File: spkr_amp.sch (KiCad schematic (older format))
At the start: 3 parts

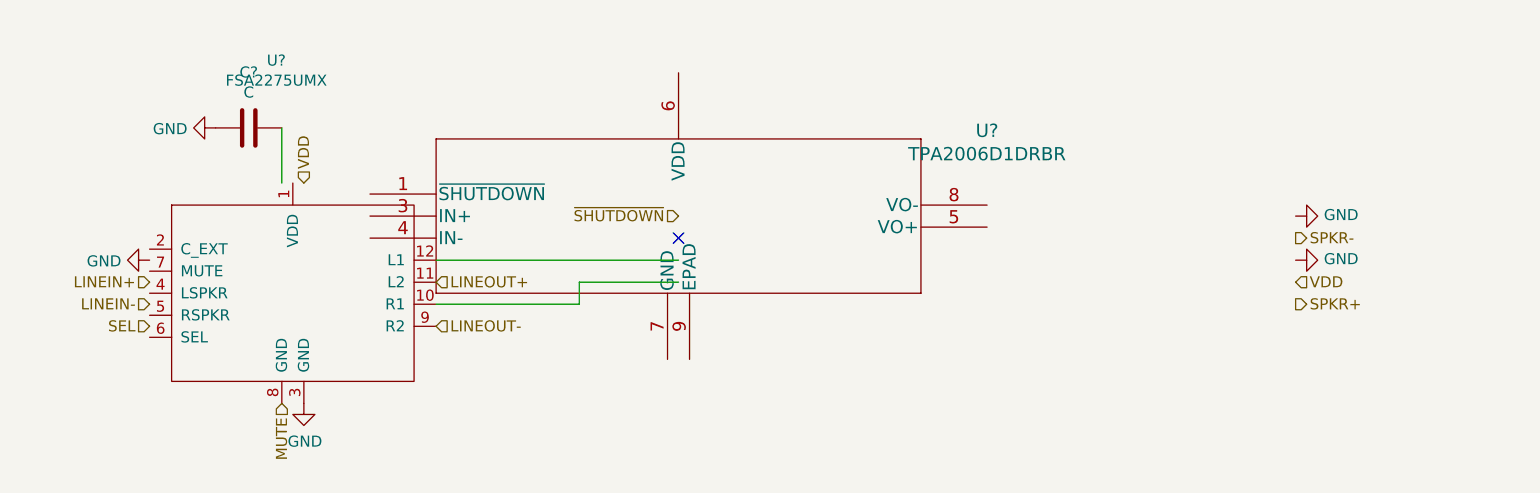
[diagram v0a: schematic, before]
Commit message: Import FSA2275 footprint from SnapEDA; annotate symbols.
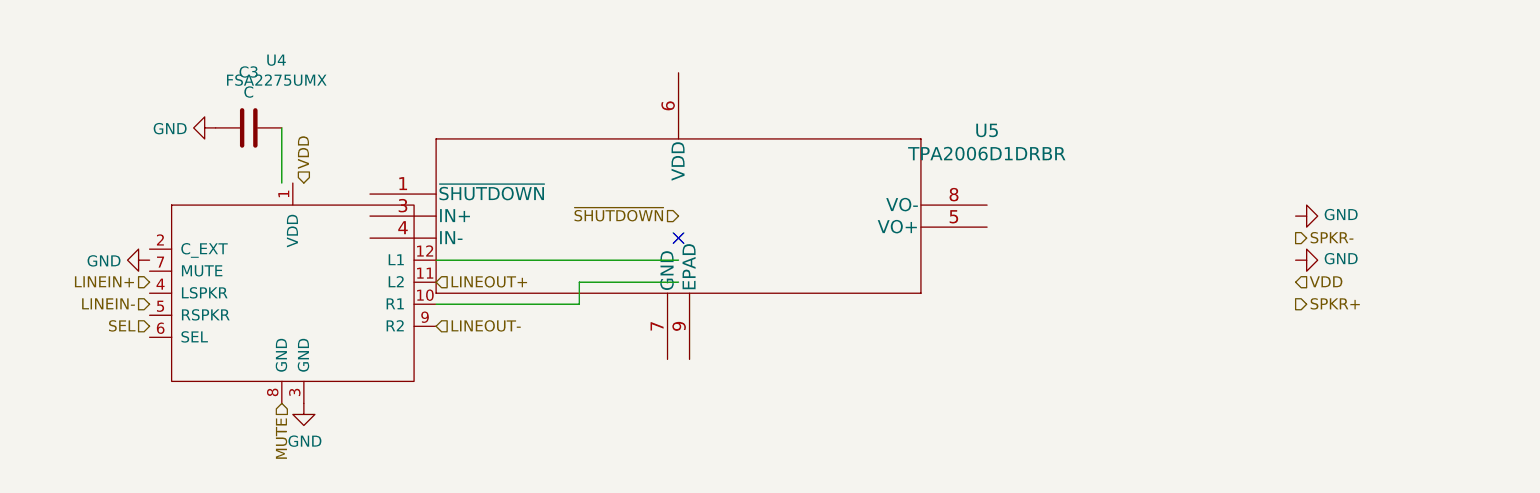
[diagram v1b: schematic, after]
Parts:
- C2: renamed from C?; footprint (none) -> Capacitor_SMD:C_0402_1005Metric
- U2: renamed from U?; footprint (none) -> footprints:FSA2275
- U3: renamed from U?; footprint DRB8_1P75X1P5 -> footprints:TPA2006D1DRBR
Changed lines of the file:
@@
 $Descr A4 11693 8268
 encoding utf-8
-Sheet 2 3
+Sheet 3 3
 Title ""
 Date ""
@@
 P 5500 3300
 AR Path="/6026AF34" Ref="U?"  Part="1"
-AR Path="/6026A3BE/6026AF34" Ref="U?"  Part="1"
-AR Path="/60276BEA/6026AF34" Ref="U?"  Part="1"
-F 0 "U?" H 6900 3687 60  0000 C CNN
+AR Path="/6026A3BE/6026AF34" Ref="U3"  Part="1"
+AR Path="/60276BEA/6026AF34" Ref="U5"  Part="1"
+F 0 "U5" H 6900 3687 60  0000 C CNN
 F 1 "TPA2006D1DRBR" H 6900 3581 60  0000 C CNN
-F 2 "DRB8_1P75X1P5" H 6900 3540 60  0001 C CNN
+F 2 "footprints:TPA2006D1DRBR" H 6900 3540 60  0001 C CNN
 F 3 "" H 5500 3300 60  0000 C CNN
 	1    5500 3300
@@
 P 3750 3650
 AR Path="/6026AF3A" Ref="U?"  Part="1"
-AR Path="/6026A3BE/6026AF3A" Ref="U?"  Part="1"
-AR Path="/60276BEA/6026AF3A" Ref="U?"  Part="1"
-F 0 "U?" H 3675 4706 50  0000 C CNN
+AR Path="/6026A3BE/6026AF3A" Ref="U2"  Part="1"
+AR Path="/60276BEA/6026AF3A" Ref="U4"  Part="1"
+F 0 "U4" H 3675 4706 50  0000 C CNN
 F 1 "FSA2275UMX" H 3675 4615 50  0000 C CNN
-F 2 "" H 3750 3650 50  0001 C CNN
+F 2 "footprints:FSA2275" H 3750 3650 50  0001 C CNN
 F 3 "" H 3750 3650 50  0001 C CNN
 	1    3750 3650
@@
 	5050 3600 5500 3600
 $Comp
-L power:GND #PWR?
+L power:GND #PWR06
 U 1 1 6027011E
 P 8300 3300
-AR Path="/6026A3BE/6027011E" Ref="#PWR?"  Part="1"
-AR Path="/60276BEA/6027011E" Ref="#PWR?"  Part="1"
-F 0 "#PWR?" H 8300 3050 50  0001 C CNN
+AR Path="/6026A3BE/6027011E" Ref="#PWR06"  Part="1"
+AR Path="/60276BEA/6027011E" Ref="#PWR011"  Part="1"
+F 0 "#PWR011" H 8300 3050 50  0001 C CNN
 F 1 "GND" V 8305 3172 50  0000 R CNN
 F 2 "" H 8300 3300 50  0001 C CNN
@@
 $EndComp
 $Comp
-L power:GND #PWR?
+L power:GND #PWR07
 U 1 1 60270A57
 P 8300 3500
-AR Path="/6026A3BE/60270A57" Ref="#PWR?"  Part="1"
-AR Path="/60276BEA/60270A57" Ref="#PWR?"  Part="1"
-F 0 "#PWR?" H 8300 3250 50  0001 C CNN
+AR Path="/6026A3BE/60270A57" Ref="#PWR07"  Part="1"
+AR Path="/60276BEA/60270A57" Ref="#PWR012"  Part="1"
+F 0 "#PWR012" H 8300 3250 50  0001 C CNN
 F 1 "GND" V 8305 3372 50  0000 R CNN
 F 2 "" H 8300 3500 50  0001 C CNN
@@
 VDD
 $Comp
-L power:GND #PWR?
+L power:GND #PWR05
 U 1 1 6027124D
 P 3800 4150
-AR Path="/6026A3BE/6027124D" Ref="#PWR?"  Part="1"
-AR Path="/60276BEA/6027124D" Ref="#PWR?"  Part="1"
-F 0 "#PWR?" H 3800 3900 50  0001 C CNN
+AR Path="/6026A3BE/6027124D" Ref="#PWR05"  Part="1"
+AR Path="/60276BEA/6027124D" Ref="#PWR010"  Part="1"
+F 0 "#PWR010" H 3800 3900 50  0001 C CNN
 F 1 "GND" H 3805 3977 50  0000 C CNN
 F 2 "" H 3800 4150 50  0001 C CNN
@@
 $EndComp
 $Comp
-L power:GND #PWR?
+L power:GND #PWR03
 U 1 1 6027187C
 P 3100 3500
-AR Path="/6026A3BE/6027187C" Ref="#PWR?"  Part="1"
-AR Path="/60276BEA/6027187C" Ref="#PWR?"  Part="1"
-F 0 "#PWR?" H 3100 3250 50  0001 C CNN
+AR Path="/6026A3BE/6027187C" Ref="#PWR03"  Part="1"
+AR Path="/60276BEA/6027187C" Ref="#PWR08"  Part="1"
+F 0 "#PWR08" H 3100 3250 50  0001 C CNN
 F 1 "GND" V 3105 3372 50  0000 R CNN
 F 2 "" H 3100 3500 50  0001 C CNN
@@
 MUTE
 $Comp
-L Device:C C?
+L Device:C C2
 U 1 1 60273CC0
 P 3550 2900
-AR Path="/6026A3BE/60273CC0" Ref="C?"  Part="1"
-AR Path="/60276BEA/60273CC0" Ref="C?"  Part="1"
-F 0 "C?" V 3298 2900 50  0000 C CNN
+AR Path="/6026A3BE/60273CC0" Ref="C2"  Part="1"
+AR Path="/60276BEA/60273CC0" Ref="C3"  Part="1"
+F 0 "C3" V 3298 2900 50  0000 C CNN
 F 1 "C" V 3389 2900 50  0000 C CNN
-F 2 "" H 3588 2750 50  0001 C CNN
+F 2 "Capacitor_SMD:C_0402_1005Metric" H 3588 2750 50  0001 C CNN
 F 3 "~" H 3550 2900 50  0001 C CNN
 	1    3550 2900
@@
 	3700 2900 3700 3150
 $Comp
-L power:GND #PWR?
+L power:GND #PWR04
 U 1 1 60274CA1
 P 3400 2900
-AR Path="/6026A3BE/60274CA1" Ref="#PWR?"  Part="1"
-AR Path="/60276BEA/60274CA1" Ref="#PWR?"  Part="1"
-F 0 "#PWR?" H 3400 2650 50  0001 C CNN
+AR Path="/6026A3BE/60274CA1" Ref="#PWR04"  Part="1"
+AR Path="/60276BEA/60274CA1" Ref="#PWR09"  Part="1"
+F 0 "#PWR09" H 3400 2650 50  0001 C CNN
 F 1 "GND" V 3405 2772 50  0000 R CNN
 F 2 "" H 3400 2900 50  0001 C CNN

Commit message: Lots more routing; set V pads on TPA2006 to GND; add 1.8V/3.3V dual LDO: TLV7111830. Save datasheets to project directory for safe keeping.
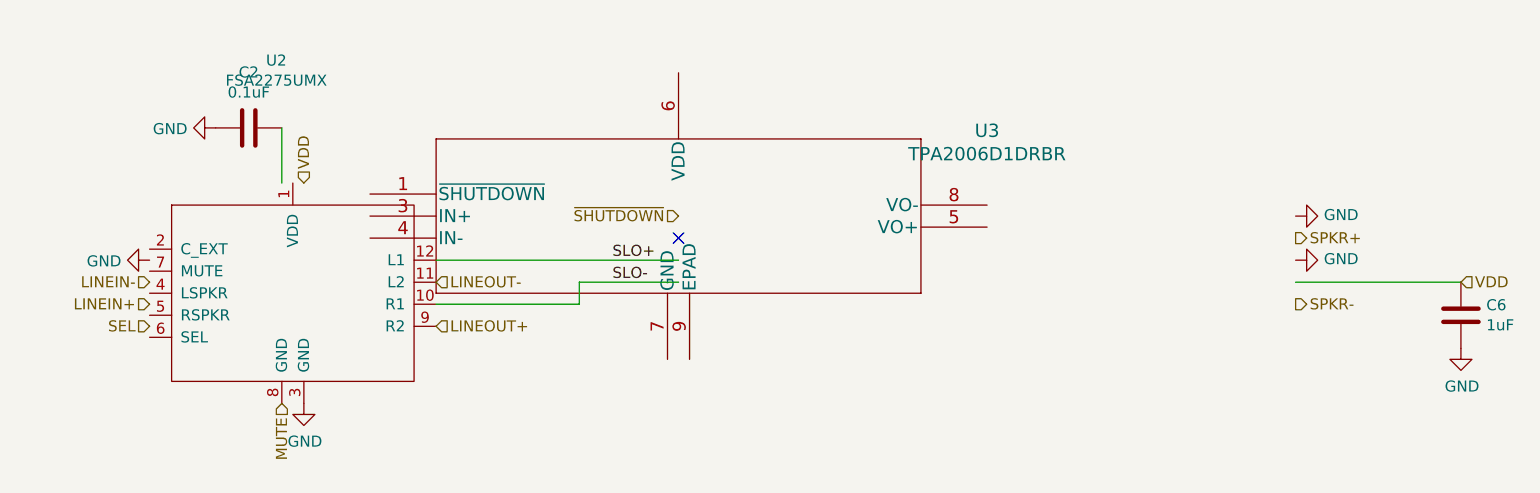
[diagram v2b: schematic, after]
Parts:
- added C7: 1uF, Capacitor_SMD:C_0402_1005Metric, symbol Device:C
- C2: value C -> 0.1uF
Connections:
- net labels added: SLO+, SLO-
- wire segments 5 -> 6
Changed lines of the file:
@@
 $Descr A4 11693 8268
 encoding utf-8
-Sheet 3 3
+Sheet 2 3
 Title ""
 Date ""
@@
 AR Path="/6026A3BE/6026AF34" Ref="U3"  Part="1"
 AR Path="/60276BEA/6026AF34" Ref="U5"  Part="1"
-F 0 "U5" H 6900 3687 60  0000 C CNN
+F 0 "U3" H 6900 3687 60  0000 C CNN
 F 1 "TPA2006D1DRBR" H 6900 3581 60  0000 C CNN
 F 2 "footprints:TPA2006D1DRBR" H 6900 3540 60  0001 C CNN
@@
 $EndComp
 $Comp
-L FSA2275UMX:FSA2275UMX U?
-U 1 1 6026AF3A
-P 3750 3650
-AR Path="/6026AF3A" Ref="U?"  Part="1"
-AR Path="/6026A3BE/6026AF3A" Ref="U2"  Part="1"
-AR Path="/60276BEA/6026AF3A" Ref="U4"  Part="1"
-F 0 "U4" H 3675 4706 50  0000 C CNN
-F 1 "FSA2275UMX" H 3675 4615 50  0000 C CNN
-F 2 "footprints:FSA2275" H 3750 3650 50  0001 C CNN
-F 3 "" H 3750 3650 50  0001 C CNN
-	1    3750 3650
-	1    0    0    -1
-$EndComp
-Wire Wire Line
-	5050 3700 5050 3600
-Wire Wire Line
-	5050 3600 5500 3600
-$Comp
 L power:GND #PWR06
 U 1 1 6027011E
@@
 AR Path="/6026A3BE/6027011E" Ref="#PWR06"  Part="1"
 AR Path="/60276BEA/6027011E" Ref="#PWR011"  Part="1"
-F 0 "#PWR011" H 8300 3050 50  0001 C CNN
+F 0 "#PWR06" H 8300 3050 50  0001 C CNN
 F 1 "GND" V 8305 3172 50  0000 R CNN
 F 2 "" H 8300 3300 50  0001 C CNN
@@
 AR Path="/6026A3BE/60270A57" Ref="#PWR07"  Part="1"
 AR Path="/60276BEA/60270A57" Ref="#PWR012"  Part="1"
-F 0 "#PWR012" H 8300 3250 50  0001 C CNN
+F 0 "#PWR07" H 8300 3250 50  0001 C CNN
 F 1 "GND" V 8305 3372 50  0000 R CNN
 F 2 "" H 8300 3500 50  0001 C CNN
@@
 $EndComp
 NoConn ~ 5500 3400
-Text HLabel 8300 3600 2    50   Input ~ 0
+Text HLabel 9050 3600 2    50   Input ~ 0
 VDD
+Text HLabel 8300 3400 2    50   Output ~ 0
+SPKR+
 Text HLabel 8300 3700 2    50   Output ~ 0
-SPKR+
-Text HLabel 8300 3400 2    50   Output ~ 0
 SPKR-
 Text HLabel 3800 3150 1    50   Input ~ 0
@@
 AR Path="/6026A3BE/6027124D" Ref="#PWR05"  Part="1"
 AR Path="/60276BEA/6027124D" Ref="#PWR010"  Part="1"
-F 0 "#PWR010" H 3800 3900 50  0001 C CNN
+F 0 "#PWR05" H 3800 3900 50  0001 C CNN
 F 1 "GND" H 3805 3977 50  0000 C CNN
 F 2 "" H 3800 4150 50  0001 C CNN
@@
 AR Path="/6026A3BE/6027187C" Ref="#PWR03"  Part="1"
 AR Path="/60276BEA/6027187C" Ref="#PWR08"  Part="1"
-F 0 "#PWR08" H 3100 3250 50  0001 C CNN
+F 0 "#PWR03" H 3100 3250 50  0001 C CNN
 F 1 "GND" V 3105 3372 50  0000 R CNN
 F 2 "" H 3100 3500 50  0001 C CNN
@@
 	0    1    1    0
 $EndComp
-Wire Wire Line
-	4400 3700 5050 3700
-Wire Wire Line
-	4400 3500 5500 3500
 Text HLabel 5500 3300 0    50   Input ~ 0
 ~SHUTDOWN
+Text HLabel 3100 3700 0    50   Input ~ 0
+LINEIN+
 Text HLabel 3100 3600 0    50   Input ~ 0
-LINEIN+
-Text HLabel 3100 3700 0    50   Input ~ 0
 LINEIN-
 Text HLabel 3100 3800 0    50   Input ~ 0
 SEL
+Text HLabel 4400 3800 2    50   Input ~ 0
+LINEOUT+
 Text HLabel 4400 3600 2    50   Input ~ 0
-LINEOUT+
-Text HLabel 4400 3800 2    50   Input ~ 0
 LINEOUT-
 Text HLabel 3700 4150 3    50   Input ~ 0
@@
 AR Path="/6026A3BE/60273CC0" Ref="C2"  Part="1"
 AR Path="/60276BEA/60273CC0" Ref="C3"  Part="1"
-F 0 "C3" V 3298 2900 50  0000 C CNN
-F 1 "C" V 3389 2900 50  0000 C CNN
+F 0 "C2" V 3298 2900 50  0000 C CNN
+F 1 "0.1uF" V 3389 2900 50  0000 C CNN
 F 2 "Capacitor_SMD:C_0402_1005Metric" H 3588 2750 50  0001 C CNN
 F 3 "~" H 3550 2900 50  0001 C CNN
@@
 AR Path="/6026A3BE/60274CA1" Ref="#PWR04"  Part="1"
 AR Path="/60276BEA/60274CA1" Ref="#PWR09"  Part="1"
-F 0 "#PWR09" H 3400 2650 50  0001 C CNN
+F 0 "#PWR04" H 3400 2650 50  0001 C CNN
 F 1 "GND" V 3405 2772 50  0000 R CNN
 F 2 "" H 3400 2900 50  0001 C CNN
@@
 	0    1    1    0
 $EndComp
+Text Label 5200 3500 0    50   ~ 0
+SLO+
+$Comp
+L FSA2275UMX:FSA2275UMX U?
+U 1 1 6026AF3A
+P 3750 3650
+AR Path="/6026AF3A" Ref="U?"  Part="1"
+AR Path="/6026A3BE/6026AF3A" Ref="U2"  Part="1"
+AR Path="/60276BEA/6026AF3A" Ref="U4"  Part="1"
+F 0 "U2" H 3675 4706 50  0000 C CNN
+F 1 "FSA2275UMX" H 3675 4615 50  0000 C CNN
+F 2 "footprints:FSA2275" H 3750 3650 50  0001 C CNN
+F 3 "" H 3750 3650 50  0001 C CNN
+	1    3750 3650
+	1    0    0    -1
+$EndComp
+Wire Wire Line
+	4400 3500 5500 3500
+Wire Wire Line
+	5500 3600 5050 3600
+Wire Wire Line
+	5050 3600 5050 3700
+Wire Wire Line
+	5050 3700 4400 3700
+Text Label 5200 3600 0    50   ~ 0
+SLO-
+$Comp
+L Device:C C7
+U 1 1 6034D245
+P 9050 3750
+AR Path="/60276BEA/6034D245" Ref="C7"  Part="1"
+AR Path="/6026A3BE/6034D245" Ref="C6"  Part="1"
+F 0 "C6" H 9165 3796 50  0000 L CNN
+F 1 "1uF" H 9165 3705 50  0000 L CNN
+F 2 "Capacitor_SMD:C_0402_1005Metric" H 9088 3600 50  0001 C CNN
+F 3 "~" H 9050 3750 50  0001 C CNN
+	1    9050 3750
+	1    0    0    -1
+$EndComp
+Wire Wire Line
+	8300 3600 9050 3600
+$Comp
+L power:GND #PWR0105
+U 1 1 6034E328
+P 9050 3900
+AR Path="/60276BEA/6034E328" Ref="#PWR0105"  Part="1"
+AR Path="/6026A3BE/6034E328" Ref="#PWR0104"  Part="1"
+F 0 "#PWR0104" H 9050 3650 50  0001 C CNN
+F 1 "GND" H 9055 3727 50  0000 C CNN
+F 2 "" H 9050 3900 50  0001 C CNN
+F 3 "" H 9050 3900 50  0001 C CNN
+	1    9050 3900
+	1    0    0    -1
+$EndComp
 $EndSCHEMATC

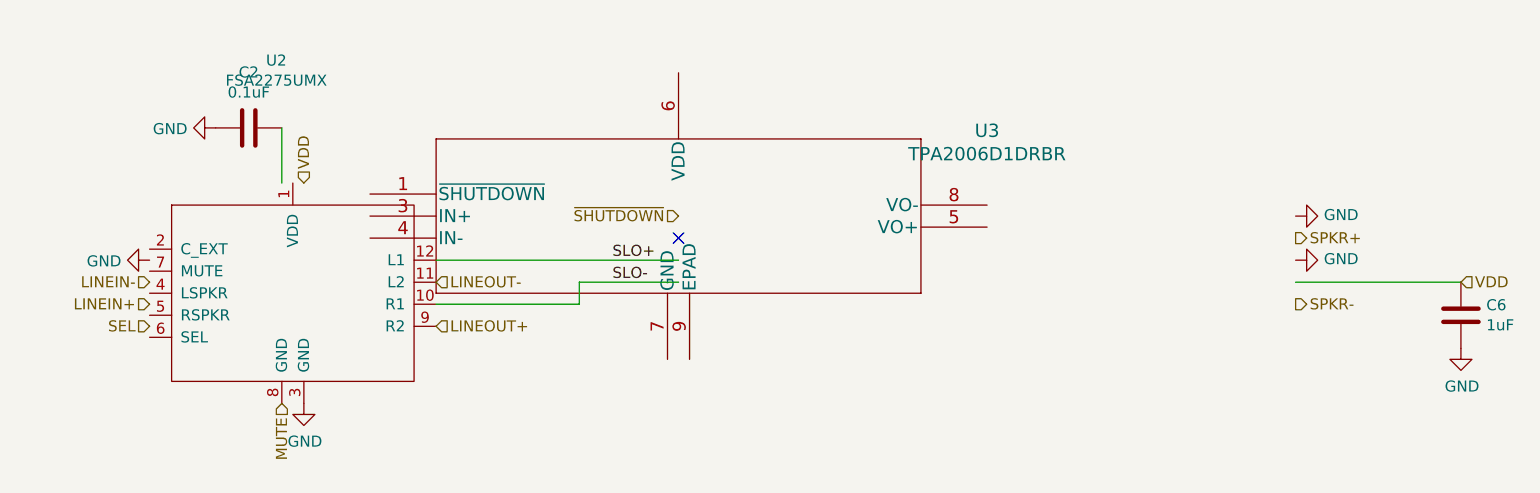
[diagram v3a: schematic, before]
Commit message: Add TVS diodes on all the headphone port pins
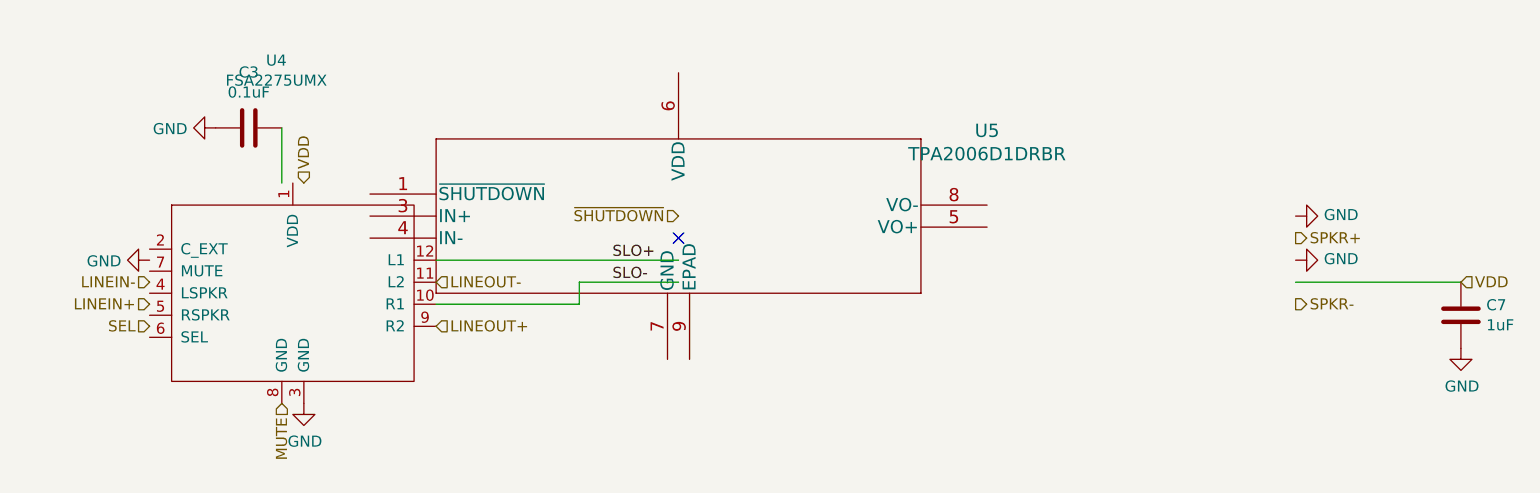
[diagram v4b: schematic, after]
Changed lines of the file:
@@
 AR Path="/6026A3BE/6026AF34" Ref="U3"  Part="1"
 AR Path="/60276BEA/6026AF34" Ref="U5"  Part="1"
-F 0 "U3" H 6900 3687 60  0000 C CNN
+F 0 "U5" H 6900 3687 60  0000 C CNN
 F 1 "TPA2006D1DRBR" H 6900 3581 60  0000 C CNN
 F 2 "footprints:TPA2006D1DRBR" H 6900 3540 60  0001 C CNN
@@
 AR Path="/6026A3BE/60273CC0" Ref="C2"  Part="1"
 AR Path="/60276BEA/60273CC0" Ref="C3"  Part="1"
-F 0 "C2" V 3298 2900 50  0000 C CNN
+F 0 "C3" V 3298 2900 50  0000 C CNN
 F 1 "0.1uF" V 3389 2900 50  0000 C CNN
 F 2 "Capacitor_SMD:C_0402_1005Metric" H 3588 2750 50  0001 C CNN
@@
 AR Path="/6026A3BE/6026AF3A" Ref="U2"  Part="1"
 AR Path="/60276BEA/6026AF3A" Ref="U4"  Part="1"
-F 0 "U2" H 3675 4706 50  0000 C CNN
+F 0 "U4" H 3675 4706 50  0000 C CNN
 F 1 "FSA2275UMX" H 3675 4615 50  0000 C CNN
 F 2 "footprints:FSA2275" H 3750 3650 50  0001 C CNN
@@
 AR Path="/60276BEA/6034D245" Ref="C7"  Part="1"
 AR Path="/6026A3BE/6034D245" Ref="C6"  Part="1"
-F 0 "C6" H 9165 3796 50  0000 L CNN
+F 0 "C7" H 9165 3796 50  0000 L CNN
 F 1 "1uF" H 9165 3705 50  0000 L CNN
 F 2 "Capacitor_SMD:C_0402_1005Metric" H 9088 3600 50  0001 C CNN

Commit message: Tidy up schematic a bit
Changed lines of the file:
@@
 $Descr A4 11693 8268
 encoding utf-8
-Sheet 2 3
+Sheet 3 3
 Title ""
 Date ""
@@
 AR Path="/6026A3BE/6026AF3A" Ref="U2"  Part="1"
 AR Path="/60276BEA/6026AF3A" Ref="U4"  Part="1"
-F 0 "U4" H 3675 4706 50  0000 C CNN
-F 1 "FSA2275UMX" H 3675 4615 50  0000 C CNN
+F 0 "U4" H 3750 3700 50  0000 C CNN
+F 1 "FSA2275UMX" H 3800 3600 50  0000 C CNN
 F 2 "footprints:FSA2275" H 3750 3650 50  0001 C CNN
 F 3 "" H 3750 3650 50  0001 C CNN
